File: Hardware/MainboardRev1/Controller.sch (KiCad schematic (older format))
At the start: 21 parts, among them Q22 NTR4003, Q23 NTR4003, Q24 NTR4003, U11 Teensy3.6

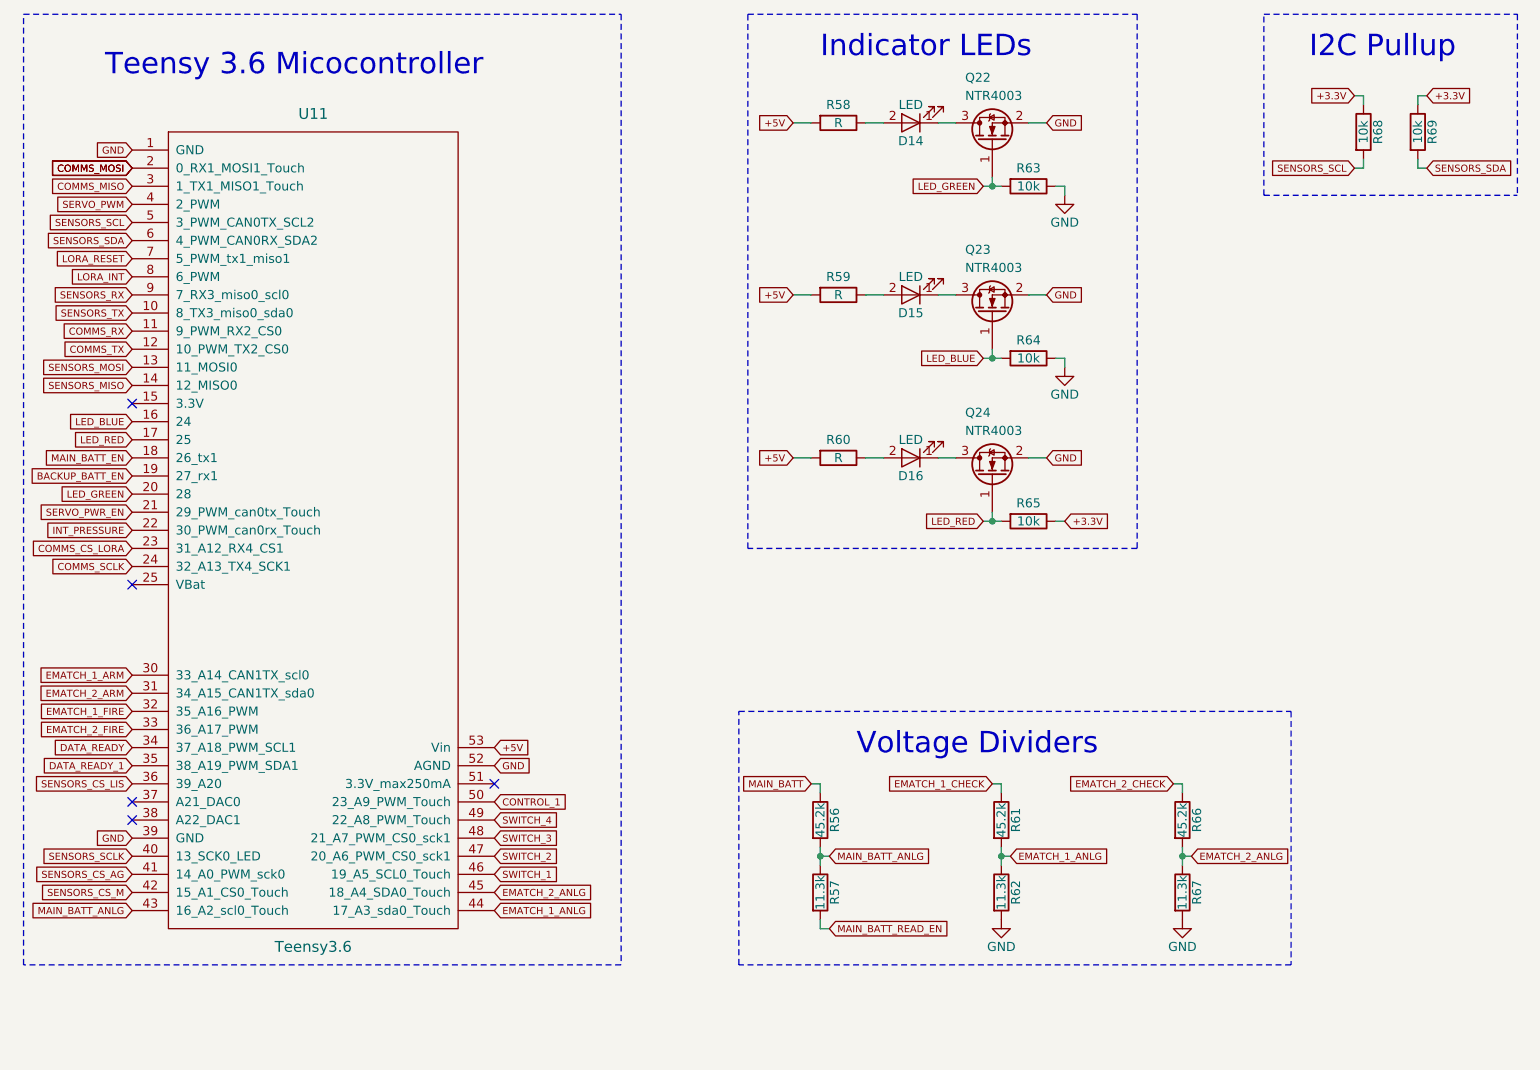
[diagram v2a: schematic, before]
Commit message: Added buzzer and strobe LED. Created BOM. Reannotated. Added sponsors to silkscreen. Needs to be routed and sent out. Good luck Matt!
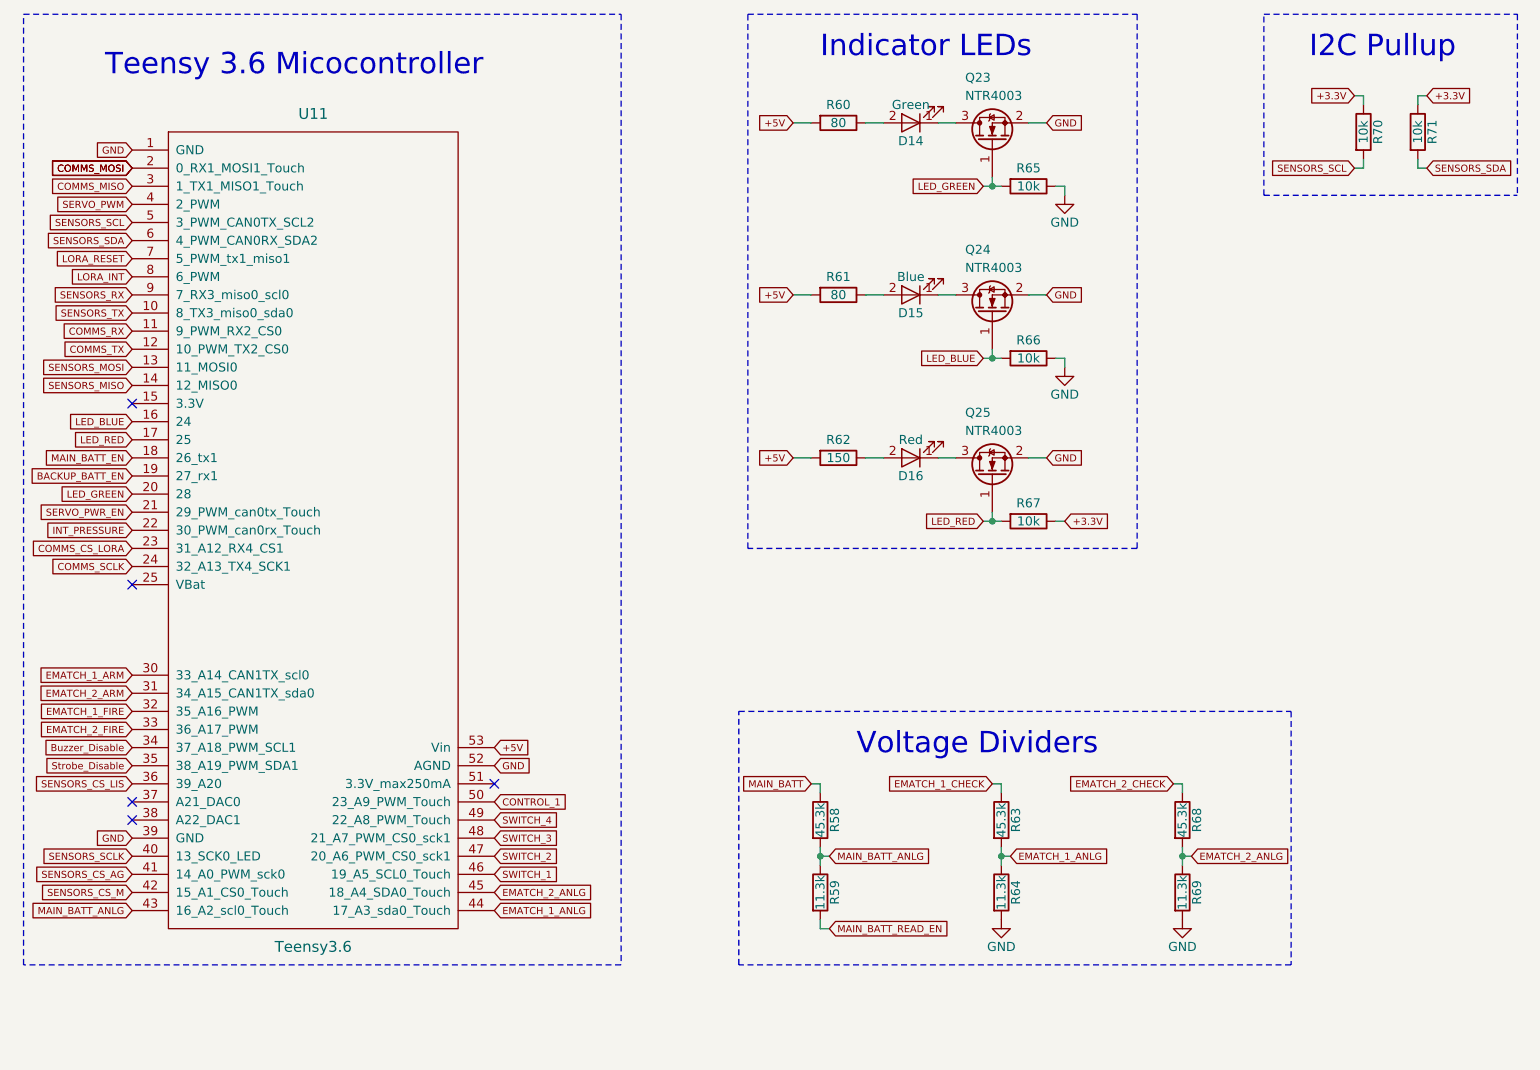
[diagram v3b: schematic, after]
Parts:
- D14: value LED -> Green
- D15: value LED -> Blue
- D16: value LED -> Red
- R58: renamed from R56; value 45.2k -> 45.3k
- R60: renamed from R58; value R -> 80
- R61: renamed from R59; value R -> 80
- R62: renamed from R60; value R -> 150
- R63: renamed from R61; value 45.2k -> 45.3k
- R68: renamed from R66; value 45.2k -> 45.3k
- renumbered Q22 to Q23, Q23 to Q24, Q24 to Q25, R57 to R59, R62 to R64, R63 to R65, R64 to R66, R65 to R67, R67 to R69, R68 to R70, R69 to R71
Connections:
- net DATA_READY renamed Buzzer_Disable
- net DATA_READY_1 renamed Strobe_Disable
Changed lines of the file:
@@
 P 6450 1450
 F 0 "D14" H 6450 1550 50  0000 C CNN
-F 1 "LED" H 6450 1350 50  0000 C CNN
+F 1 "Green" H 6450 1350 50  0000 C CNN
 F 2 "LEDs:LED_0603_HandSoldering" H 6450 1450 50  0001 C CNN
 F 3 "" H 6450 1450 50  0001 C CNN
@@
 $EndComp
 $Comp
-L Q_NMOS_GSD Q22
+L Q_NMOS_GSD Q23
 U 1 1 5AFD5288
 P 6900 1550
-F 0 "Q22" V 7250 1700 50  0000 R CNN
+F 0 "Q23" V 7250 1700 50  0000 R CNN
 F 1 "NTR4003" V 7150 1700 50  0000 R CNN
 F 2 "TO_SOT_Packages_SMD:SOT-23" H 7100 1650 50  0001 C CNN
@@
 GND
 $Comp
-L R R58
+L R R60
 U 1 1 5AFD53B2
 P 6050 1450
-F 0 "R58" V 5950 1450 50  0000 C CNN
-F 1 "R" V 6050 1450 50  0000 C CNN
+F 0 "R60" V 5950 1450 50  0000 C CNN
+F 1 "80" V 6050 1450 50  0000 C CNN
 F 2 "Resistors_SMD:R_0603_HandSoldering" V 5980 1450 50  0001 C CNN
 F 3 "" H 6050 1450 50  0001 C CNN
@@
 LED_GREEN
 $Comp
-L R R63
+L R R65
 U 1 1 5AFD592A
 P 7100 1800
-F 0 "R63" V 7000 1800 50  0000 C CNN
+F 0 "R65" V 7000 1800 50  0000 C CNN
 F 1 "10k" V 7100 1800 50  0000 C CNN
 F 2 "Resistors_SMD:R_0603_HandSoldering" V 7030 1800 50  0001 C CNN
@@
 Connection ~ 6900 1800
 $Comp
-L GND #PWR052
+L GND #PWR050
 U 1 1 5AFD5996
 P 7300 1850
-F 0 "#PWR052" H 7300 1600 50  0001 C CNN
+F 0 "#PWR050" H 7300 1600 50  0001 C CNN
 F 1 "GND" H 7300 1700 50  0000 C CNN
 F 2 "" H 7300 1850 50  0001 C CNN
@@
 P 6450 2400
 F 0 "D15" H 6450 2500 50  0000 C CNN
-F 1 "LED" H 6450 2300 50  0000 C CNN
+F 1 "Blue" H 6450 2300 50  0000 C CNN
 F 2 "LEDs:LED_0603_HandSoldering" H 6450 2400 50  0001 C CNN
 F 3 "" H 6450 2400 50  0001 C CNN
@@
 $EndComp
 $Comp
-L Q_NMOS_GSD Q23
+L Q_NMOS_GSD Q24
 U 1 1 5AFD5ABC
 P 6900 2500
-F 0 "Q23" V 7250 2650 50  0000 R CNN
+F 0 "Q24" V 7250 2650 50  0000 R CNN
 F 1 "NTR4003" V 7150 2650 50  0000 R CNN
 F 2 "TO_SOT_Packages_SMD:SOT-23" H 7100 2600 50  0001 C CNN
@@
 GND
 $Comp
-L R R59
+L R R61
 U 1 1 5AFD5AC4
 P 6050 2400
-F 0 "R59" V 5950 2400 50  0000 C CNN
-F 1 "R" V 6050 2400 50  0000 C CNN
+F 0 "R61" V 5950 2400 50  0000 C CNN
+F 1 "80" V 6050 2400 50  0000 C CNN
 F 2 "Resistors_SMD:R_0603_HandSoldering" V 5980 2400 50  0001 C CNN
 F 3 "" H 6050 2400 50  0001 C CNN
@@
 LED_BLUE
 $Comp
-L R R64
+L R R66
 U 1 1 5AFD5ACF
 P 7100 2750
-F 0 "R64" V 7000 2750 50  0000 C CNN
+F 0 "R66" V 7000 2750 50  0000 C CNN
 F 1 "10k" V 7100 2750 50  0000 C CNN
 F 2 "Resistors_SMD:R_0603_HandSoldering" V 7030 2750 50  0001 C CNN
@@
 Connection ~ 6900 2750
 $Comp
-L GND #PWR053
+L GND #PWR051
 U 1 1 5AFD5AD8
 P 7300 2800
-F 0 "#PWR053" H 7300 2550 50  0001 C CNN
+F 0 "#PWR051" H 7300 2550 50  0001 C CNN
 F 1 "GND" H 7300 2650 50  0000 C CNN
 F 2 "" H 7300 2800 50  0001 C CNN
@@
 P 6450 3300
 F 0 "D16" H 6450 3400 50  0000 C CNN
-F 1 "LED" H 6450 3200 50  0000 C CNN
+F 1 "Red" H 6450 3200 50  0000 C CNN
 F 2 "LEDs:LED_0603_HandSoldering" H 6450 3300 50  0001 C CNN
 F 3 "" H 6450 3300 50  0001 C CNN
@@
 $EndComp
 $Comp
-L Q_NMOS_GSD Q24
+L Q_NMOS_GSD Q25
 U 1 1 5AFD5BDF
 P 6900 3400
-F 0 "Q24" V 7250 3550 50  0000 R CNN
+F 0 "Q25" V 7250 3550 50  0000 R CNN
 F 1 "NTR4003" V 7150 3550 50  0000 R CNN
 F 2 "TO_SOT_Packages_SMD:SOT-23" H 7100 3500 50  0001 C CNN
@@
 GND
 $Comp
-L R R60
+L R R62
 U 1 1 5AFD5BE7
 P 6050 3300
-F 0 "R60" V 5950 3300 50  0000 C CNN
-F 1 "R" V 6050 3300 50  0000 C CNN
+F 0 "R62" V 5950 3300 50  0000 C CNN
+F 1 "150" V 6050 3300 50  0000 C CNN
 F 2 "Resistors_SMD:R_0603_HandSoldering" V 5980 3300 50  0001 C CNN
 F 3 "" H 6050 3300 50  0001 C CNN
@@
 LED_RED
 $Comp
-L R R65
+L R R67
 U 1 1 5AFD5BF2
 P 7100 3650
-F 0 "R65" V 7000 3650 50  0000 C CNN
+F 0 "R67" V 7000 3650 50  0000 C CNN
 F 1 "10k" V 7100 3650 50  0000 C CNN
 F 2 "Resistors_SMD:R_0603_HandSoldering" V 7030 3650 50  0001 C CNN
@@
 	8950 1700 8950 1650
 $Comp
-L R R68
+L R R70
 U 1 1 5AFD610C
 P 8950 1500
-F 0 "R68" V 9030 1500 50  0000 C CNN
+F 0 "R70" V 9030 1500 50  0000 C CNN
 F 1 "10k" V 8950 1500 50  0000 C CNN
 F 2 "Resistors_SMD:R_0603_HandSoldering" V 8880 1500 50  0001 C CNN
@@
 	8950 1300 8950 1350
 $Comp
-L R R69
+L R R71
 U 1 1 5AFD61B1
 P 9250 1500
-F 0 "R69" V 9330 1500 50  0000 C CNN
+F 0 "R71" V 9330 1500 50  0000 C CNN
 F 1 "10k" V 9250 1500 50  0000 C CNN
 F 2 "Resistors_SMD:R_0603_HandSoldering" V 9180 1500 50  0001 C CNN
@@
 	9800 850  9800 1850
 Text GLabel 2150 4900 0    39   Input ~ 0
-DATA_READY
+Buzzer_Disable
 Text GLabel 2150 5000 0    39   Input ~ 0
-DATA_READY_1
+Strobe_Disable
 Text Notes 6150 4950 0    118  ~ 0
 Voltage Dividers
 $Comp
-L R R56
+L R R58
 U 1 1 5AFCDCCB
 P 5950 5300
-F 0 "R56" V 6030 5300 50  0000 C CNN
-F 1 "45.2k" V 5950 5300 50  0000 C CNN
+F 0 "R58" V 6030 5300 50  0000 C CNN
+F 1 "45.3k" V 5950 5300 50  0000 C CNN
 F 2 "Resistors_SMD:R_0603_HandSoldering" V 5880 5300 50  0001 C CNN
 F 3 "" H 5950 5300 50  0001 C CNN
@@
 $EndComp
 $Comp
-L R R57
+L R R59
 U 1 1 5AFCDD5E
 P 5950 5700
-F 0 "R57" V 6030 5700 50  0000 C CNN
+F 0 "R59" V 6030 5700 50  0000 C CNN
 F 1 "11.3k" V 5950 5700 50  0000 C CNN
 F 2 "Resistors_SMD:R_0603_HandSoldering" V 5880 5700 50  0001 C CNN
@@
 EMATCH_1_CHECK
 $Comp
-L R R61
+L R R63
 U 1 1 5AFD293E
 P 6950 5300
-F 0 "R61" V 7030 5300 50  0000 C CNN
-F 1 "45.2k" V 6950 5300 50  0000 C CNN
+F 0 "R63" V 7030 5300 50  0000 C CNN
+F 1 "45.3k" V 6950 5300 50  0000 C CNN
 F 2 "Resistors_SMD:R_0603_HandSoldering" V 6880 5300 50  0001 C CNN
 F 3 "" H 6950 5300 50  0001 C CNN
@@
 $EndComp
 $Comp
-L R R62
+L R R64
 U 1 1 5AFD2944
 P 6950 5700
-F 0 "R62" V 7030 5700 50  0000 C CNN
+F 0 "R64" V 7030 5700 50  0000 C CNN
 F 1 "11.3k" V 6950 5700 50  0000 C CNN
 F 2 "Resistors_SMD:R_0603_HandSoldering" V 6880 5700 50  0001 C CNN
@@
 Connection ~ 6950 5500
 $Comp
-L GND #PWR054
+L GND #PWR052
 U 1 1 5AFD29A3
 P 6950 5850
-F 0 "#PWR054" H 6950 5600 50  0001 C CNN
+F 0 "#PWR052" H 6950 5600 50  0001 C CNN
 F 1 "GND" H 6950 5700 50  0000 C CNN
 F 2 "" H 6950 5850 50  0001 C CNN
@@
 EMATCH_2_CHECK
 $Comp
-L R R66
+L R R68
 U 1 1 5AFD2CA4
 P 7950 5300
-F 0 "R66" V 8030 5300 50  0000 C CNN
-F 1 "45.2k" V 7950 5300 50  0000 C CNN
+F 0 "R68" V 8030 5300 50  0000 C CNN
+F 1 "45.3k" V 7950 5300 50  0000 C CNN
 F 2 "Resistors_SMD:R_0603_HandSoldering" V 7880 5300 50  0001 C CNN
 F 3 "" H 7950 5300 50  0001 C CNN
@@
 $EndComp
 $Comp
-L R R67
+L R R69
 U 1 1 5AFD2CAA
 P 7950 5700
-F 0 "R67" V 8030 5700 50  0000 C CNN
+F 0 "R69" V 8030 5700 50  0000 C CNN
 F 1 "11.3k" V 7950 5700 50  0000 C CNN
 F 2 "Resistors_SMD:R_0603_HandSoldering" V 7880 5700 50  0001 C CNN
@@
 Connection ~ 7950 5500
 $Comp
-L GND #PWR055
+L GND #PWR053
 U 1 1 5AFD2CB6
 P 7950 5850
-F 0 "#PWR055" H 7950 5600 50  0001 C CNN
+F 0 "#PWR053" H 7950 5600 50  0001 C CNN
 F 1 "GND" H 7950 5700 50  0000 C CNN
 F 2 "" H 7950 5850 50  0001 C CNN
